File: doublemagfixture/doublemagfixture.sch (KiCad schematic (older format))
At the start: 36 parts, among them J1 Barrel_Jack_MountingPin, J2 Screw_Terminal_01x04, J3 Screw_Terminal_01x04, J4 Screw_Terminal_01x04, J5 Screw_Terminal_01x04, J6 Screw_Terminal_01x08, J7 Screw_Terminal_01x08, M1 12V_350mA_Stepper_Motor, M2 12V_350mA_Stepper_Motor, M3 12V_350mA_Stepper_Motor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

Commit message: almost done pcb
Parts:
- added H1, H2, H3: MountingHole, MountingHole:MountingHole_3.2mm_M3_Pad, symbol Mechanical:MountingHole
- D1: value DIR_IND -> DIR0
- D2: value DIR_IND -> DIR1
- D3: value STEP_IND -> STEP0
- D4: value STEP_IND -> STEP1
- D5: value DIR_IND -> DIR2
- D6: value DIR_IND -> DIR3
- D7: value STEP_IND -> STEP2
- D8: value STEP_IND -> STEP3
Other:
- note added: "to fixture"
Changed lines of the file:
@@
 EESchema Schematic File Version 4
-LIBS:doublemagfixture-cache
 EELAYER 30 0
 EELAYER END
@@
 P 7450 1100
 F 0 "D1" H 7450 893 50  0000 C CNN
-F 1 "DIR_IND" H 7450 984 50  0000 C CNN
+F 1 "DIR0" H 7450 984 50  0000 C CNN
 F 2 "LED_THT:LED_D3.0mm" V 7450 1100 50  0001 C CNN
 F 3 "~" V 7450 1100 50  0001 C CNN
@@
 P 7450 1200
 F 0 "D3" H 7450 1400 50  0000 C CNN
-F 1 "STEP_IND" H 7450 1300 50  0000 C CNN
+F 1 "STEP0" H 7450 1300 50  0000 C CNN
 F 2 "LED_THT:LED_D3.0mm" V 7450 1200 50  0001 C CNN
 F 3 "~" V 7450 1200 50  0001 C CNN
@@
 P 10750 1100
 F 0 "D2" H 10750 893 50  0000 C CNN
-F 1 "DIR_IND" H 10750 984 50  0000 C CNN
+F 1 "DIR1" H 10750 984 50  0000 C CNN
 F 2 "LED_THT:LED_D3.0mm" V 10750 1100 50  0001 C CNN
 F 3 "~" V 10750 1100 50  0001 C CNN
@@
 P 10750 1200
 F 0 "D4" H 10750 1400 50  0000 C CNN
-F 1 "STEP_IND" H 10750 1300 50  0000 C CNN
+F 1 "STEP1" H 10750 1300 50  0000 C CNN
 F 2 "LED_THT:LED_D3.0mm" V 10750 1200 50  0001 C CNN
 F 3 "~" V 10750 1200 50  0001 C CNN
@@
 P 7500 3700
 F 0 "D5" H 7500 3493 50  0000 C CNN
-F 1 "DIR_IND" H 7500 3584 50  0000 C CNN
+F 1 "DIR2" H 7500 3584 50  0000 C CNN
 F 2 "LED_THT:LED_D3.0mm" V 7500 3700 50  0001 C CNN
 F 3 "~" V 7500 3700 50  0001 C CNN
@@
 P 7500 3800
 F 0 "D7" H 7500 4000 50  0000 C CNN
-F 1 "STEP_IND" H 7500 3900 50  0000 C CNN
+F 1 "STEP2" H 7500 3900 50  0000 C CNN
 F 2 "LED_THT:LED_D3.0mm" V 7500 3800 50  0001 C CNN
 F 3 "~" V 7500 3800 50  0001 C CNN
@@
 P 10800 3700
 F 0 "D6" H 10800 3493 50  0000 C CNN
-F 1 "DIR_IND" H 10800 3584 50  0000 C CNN
+F 1 "DIR3" H 10800 3584 50  0000 C CNN
 F 2 "LED_THT:LED_D3.0mm" V 10800 3700 50  0001 C CNN
 F 3 "~" V 10800 3700 50  0001 C CNN
@@
 P 10800 3800
 F 0 "D8" H 10800 4000 50  0000 C CNN
-F 1 "STEP_IND" H 10800 3900 50  0000 C CNN
+F 1 "STEP3" H 10800 3900 50  0000 C CNN
 F 2 "LED_THT:LED_D3.0mm" V 10800 3800 50  0001 C CNN
 F 3 "~" V 10800 3800 50  0001 C CNN
@@
 Text Notes 1650 3600 2    50   ~ 0
 to limit switch
+Text Notes 5350 3000 0    50   ~ 0
+to fixture
+Text Notes 5400 5600 0    50   ~ 0
+to fixture
+Text Notes 8700 5600 0    50   ~ 0
+to fixture
+Text Notes 8650 3000 0    50   ~ 0
+to fixture
+$Comp
+L Mechanical:MountingHole H1
+U 1 1 61660AAE
+P 700 700
+F 0 "H1" H 800 746 50  0000 L CNN
+F 1 "MountingHole" H 800 655 50  0000 L CNN
+F 2 "MountingHole:MountingHole_3.2mm_M3_Pad" H 700 700 50  0001 C CNN
+F 3 "~" H 700 700 50  0001 C CNN
+	1    700  700
+	1    0    0    -1
+$EndComp
+$Comp
+L Mechanical:MountingHole H2
+U 1 1 6166153D
+P 700 950
+F 0 "H2" H 800 996 50  0000 L CNN
+F 1 "MountingHole" H 800 905 50  0000 L CNN
+F 2 "MountingHole:MountingHole_3.2mm_M3_Pad" H 700 950 50  0001 C CNN
+F 3 "~" H 700 950 50  0001 C CNN
+	1    700  950
+	1    0    0    -1
+$EndComp
+$Comp
+L Mechanical:MountingHole H3
+U 1 1 616617E1
+P 700 1200
+F 0 "H3" H 800 1246 50  0000 L CNN
+F 1 "MountingHole" H 800 1155 50  0000 L CNN
+F 2 "MountingHole:MountingHole_3.2mm_M3_Pad" H 700 1200 50  0001 C CNN
+F 3 "~" H 700 1200 50  0001 C CNN
+	1    700  1200
+	1    0    0    -1
+$EndComp
 $EndSCHEMATC

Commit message: Final(?) pcb
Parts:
- renumbered M3 to M2, M2 to M3
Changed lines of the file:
@@
 	2550 6900 2650 6900
 Connection ~ 2650 6900
-Wire Wire Line
-	2650 6900 2750 6900
 $Comp
 L Motor:Stepper_Motor_bipolar M1
@@
 $EndComp
 Wire Wire Line
-	8850 1100 8450 1100
-Wire Wire Line
 	8450 1100 8450 1000
 $Comp
@@
 	4950 2300 4500 2300
 $Comp
-L Motor:Stepper_Motor_bipolar M2
+L Motor:Stepper_Motor_bipolar M3
 U 1 1 619BDAE8
 P 4450 5400
-F 0 "M2" V 4650 5450 50  0000 R CNN
+F 0 "M3" V 4650 5450 50  0000 R CNN
 F 1 "12V_350mA_Stepper_Motor" V 4750 5900 50  0000 R CNN
 F 2 "" H 4460 5390 50  0001 C CNN
@@
 	8300 4900 7850 4900
 $Comp
-L Motor:Stepper_Motor_bipolar M3
+L Motor:Stepper_Motor_bipolar M2
 U 1 1 619CD0F7
 P 7700 2800
-F 0 "M3" V 7900 2850 50  0000 R CNN
+F 0 "M2" V 7900 2850 50  0000 R CNN
 F 1 "12V_350mA_Stepper_Motor" V 8000 3300 50  0000 R CNN
 F 2 "" H 7710 2790 50  0001 C CNN
@@
 	1    0    0    -1
 $EndComp
+Wire Wire Line
+	8850 1100 8450 1100
+Wire Wire Line
+	2750 6900 2650 6900
 $EndSCHEMATC

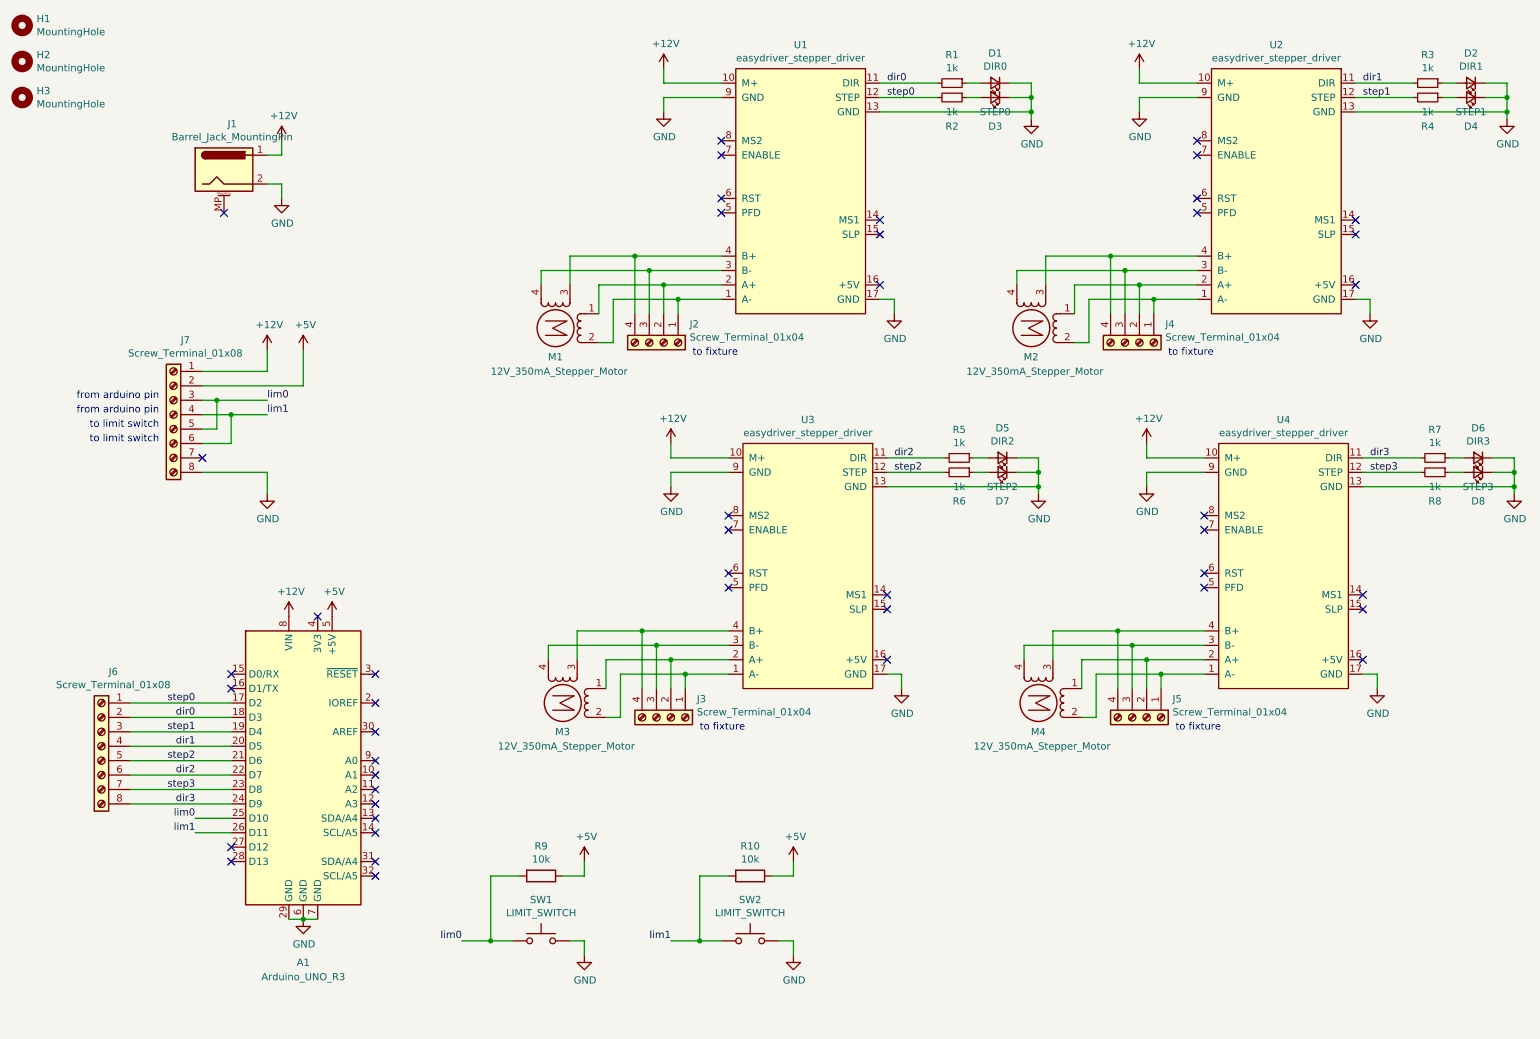
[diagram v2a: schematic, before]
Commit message: numbering fixes and wider traces on power line
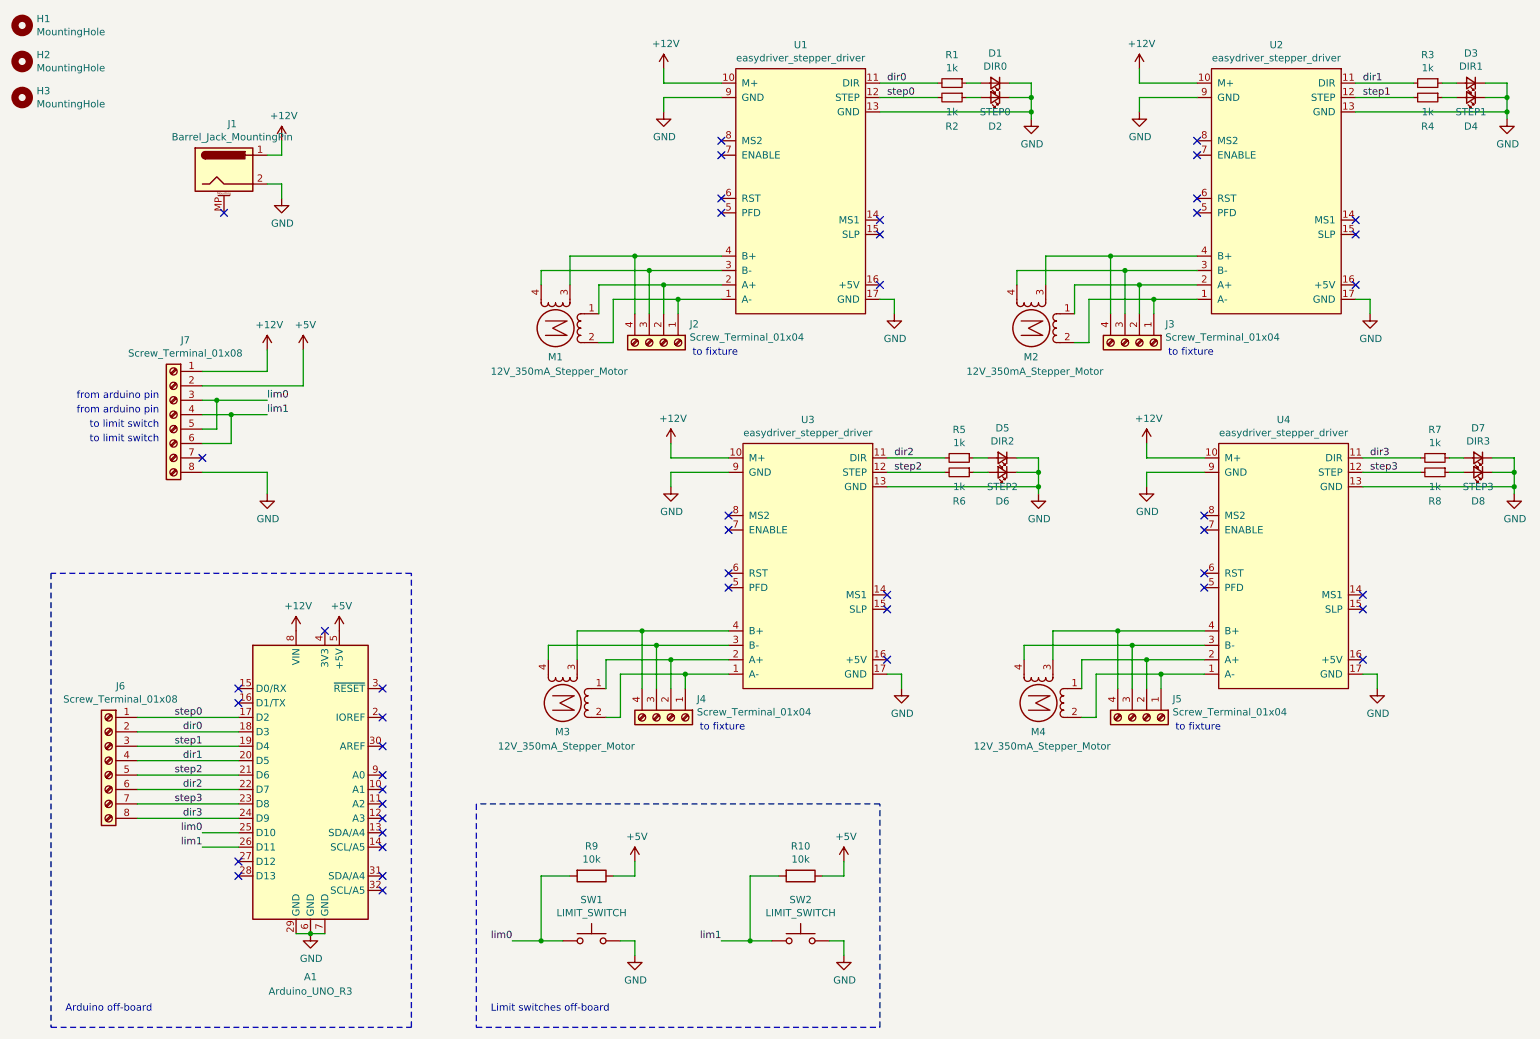
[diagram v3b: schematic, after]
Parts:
- renumbered D3 to D2, D2 to D3, D7 to D6, D6 to D7, J4 to J3, J3 to J4
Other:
- note added: "Arduino off-board"
- note added: "Limit switches off-board"
- moved on the sheet: A1, J6, R10, R9, SW1, SW2

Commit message: change LED to 5mm
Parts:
- D1, D2, D3, D4, D5, D6, D7, D8: footprint LED_THT:LED_D3.0mm -> LED_THT:LED_D5.0mm
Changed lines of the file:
@@
 F 0 "D1" H 7450 893 50  0000 C CNN
 F 1 "DIR0" H 7450 984 50  0000 C CNN
-F 2 "LED_THT:LED_D3.0mm" V 7450 1100 50  0001 C CNN
+F 2 "LED_THT:LED_D5.0mm" V 7450 1100 50  0001 C CNN
 F 3 "~" V 7450 1100 50  0001 C CNN
 	1    7450 1100
@@
 F 0 "D2" H 7450 1400 50  0000 C CNN
 F 1 "STEP0" H 7450 1300 50  0000 C CNN
-F 2 "LED_THT:LED_D3.0mm" V 7450 1200 50  0001 C CNN
+F 2 "LED_THT:LED_D5.0mm" V 7450 1200 50  0001 C CNN
 F 3 "~" V 7450 1200 50  0001 C CNN
 	1    7450 1200
@@
 F 0 "D3" H 10750 893 50  0000 C CNN
 F 1 "DIR1" H 10750 984 50  0000 C CNN
-F 2 "LED_THT:LED_D3.0mm" V 10750 1100 50  0001 C CNN
+F 2 "LED_THT:LED_D5.0mm" V 10750 1100 50  0001 C CNN
 F 3 "~" V 10750 1100 50  0001 C CNN
 	1    10750 1100
@@
 F 0 "D4" H 10750 1400 50  0000 C CNN
 F 1 "STEP1" H 10750 1300 50  0000 C CNN
-F 2 "LED_THT:LED_D3.0mm" V 10750 1200 50  0001 C CNN
+F 2 "LED_THT:LED_D5.0mm" V 10750 1200 50  0001 C CNN
 F 3 "~" V 10750 1200 50  0001 C CNN
 	1    10750 1200
@@
 F 0 "D5" H 7500 3493 50  0000 C CNN
 F 1 "DIR2" H 7500 3584 50  0000 C CNN
-F 2 "LED_THT:LED_D3.0mm" V 7500 3700 50  0001 C CNN
+F 2 "LED_THT:LED_D5.0mm" V 7500 3700 50  0001 C CNN
 F 3 "~" V 7500 3700 50  0001 C CNN
 	1    7500 3700
@@
 F 0 "D6" H 7500 4000 50  0000 C CNN
 F 1 "STEP2" H 7500 3900 50  0000 C CNN
-F 2 "LED_THT:LED_D3.0mm" V 7500 3800 50  0001 C CNN
+F 2 "LED_THT:LED_D5.0mm" V 7500 3800 50  0001 C CNN
 F 3 "~" V 7500 3800 50  0001 C CNN
 	1    7500 3800
@@
 F 0 "D7" H 10800 3493 50  0000 C CNN
 F 1 "DIR3" H 10800 3584 50  0000 C CNN
-F 2 "LED_THT:LED_D3.0mm" V 10800 3700 50  0001 C CNN
+F 2 "LED_THT:LED_D5.0mm" V 10800 3700 50  0001 C CNN
 F 3 "~" V 10800 3700 50  0001 C CNN
 	1    10800 3700
@@
 F 0 "D8" H 10800 4000 50  0000 C CNN
 F 1 "STEP3" H 10800 3900 50  0000 C CNN
-F 2 "LED_THT:LED_D3.0mm" V 10800 3800 50  0001 C CNN
+F 2 "LED_THT:LED_D5.0mm" V 10800 3800 50  0001 C CNN
 F 3 "~" V 10800 3800 50  0001 C CNN
 	1    10800 3800

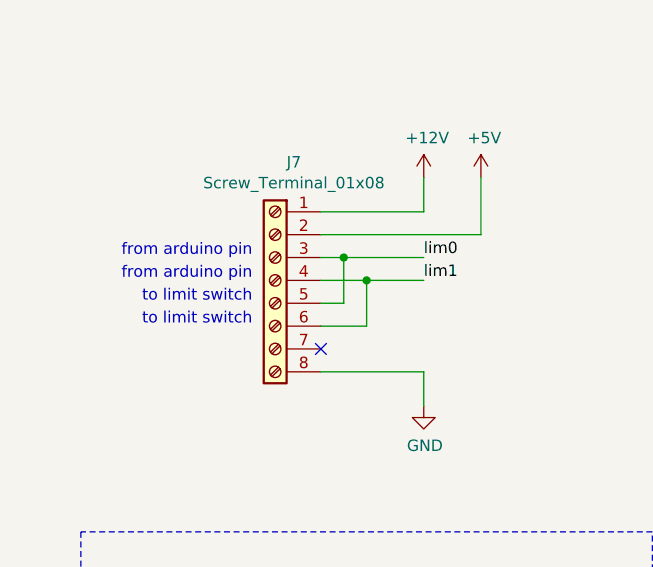
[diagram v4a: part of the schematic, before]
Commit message: add breakout board and reconfigure main board
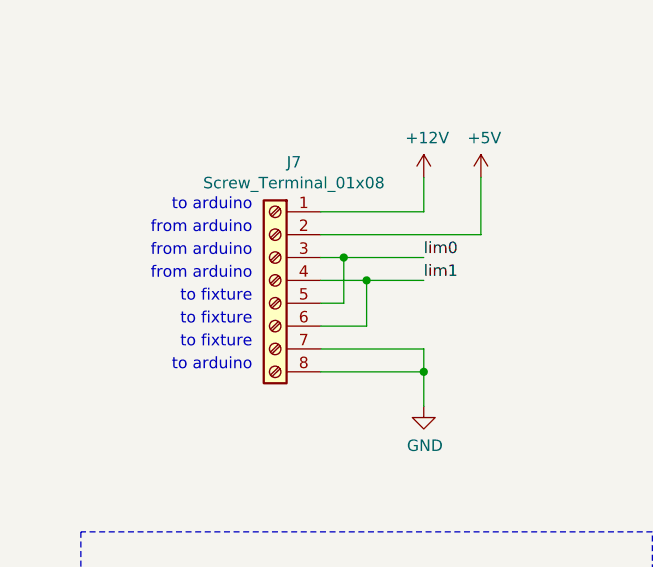
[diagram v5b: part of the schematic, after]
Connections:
- net GND: now also J7.7 (Pin_7)
- no-connect marks 46 -> 45
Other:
- note added: "from arduino"
- note added: "to arduino"
- note removed: "from arduino pin"
- note removed: "to limit switch"
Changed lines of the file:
@@
 Wire Wire Line
 	2150 3400 1950 3400
-NoConn ~ 1950 3700
 Text Notes 1650 3300 2    50   ~ 0
-from arduino pin
+from arduino
 Text Notes 1650 3400 2    50   ~ 0
-from arduino pin
+from arduino
 Text Notes 1650 3500 2    50   ~ 0
-to limit switch
+to fixture
 Text Notes 1650 3600 2    50   ~ 0
-to limit switch
+to fixture
 Text Notes 5350 3000 0    50   ~ 0
 to fixture
@@
 Wire Notes Line
 	900  7650 3400 7650
+Wire Wire Line
+	1950 3700 2400 3700
+Wire Wire Line
+	2400 3700 2400 3800
+Connection ~ 2400 3800
+Text Notes 1650 3700 2    50   ~ 0
+to fixture
+Text Notes 1650 3100 2    50   ~ 0
+to arduino
+Text Notes 1650 3200 2    50   ~ 0
+from arduino
+Text Notes 1650 3800 2    50   ~ 0
+to arduino
 $EndSCHEMATC

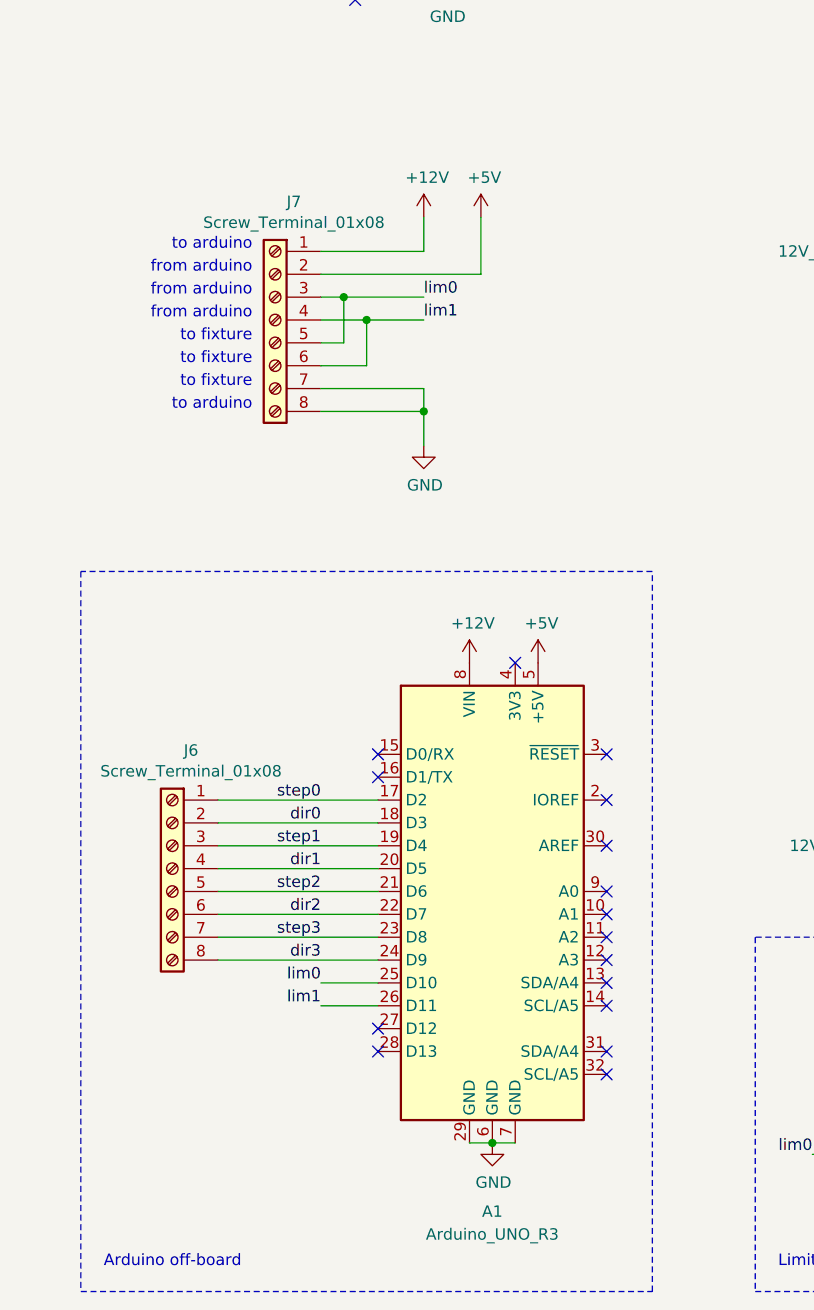
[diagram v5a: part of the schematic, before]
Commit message: add 3D mag work
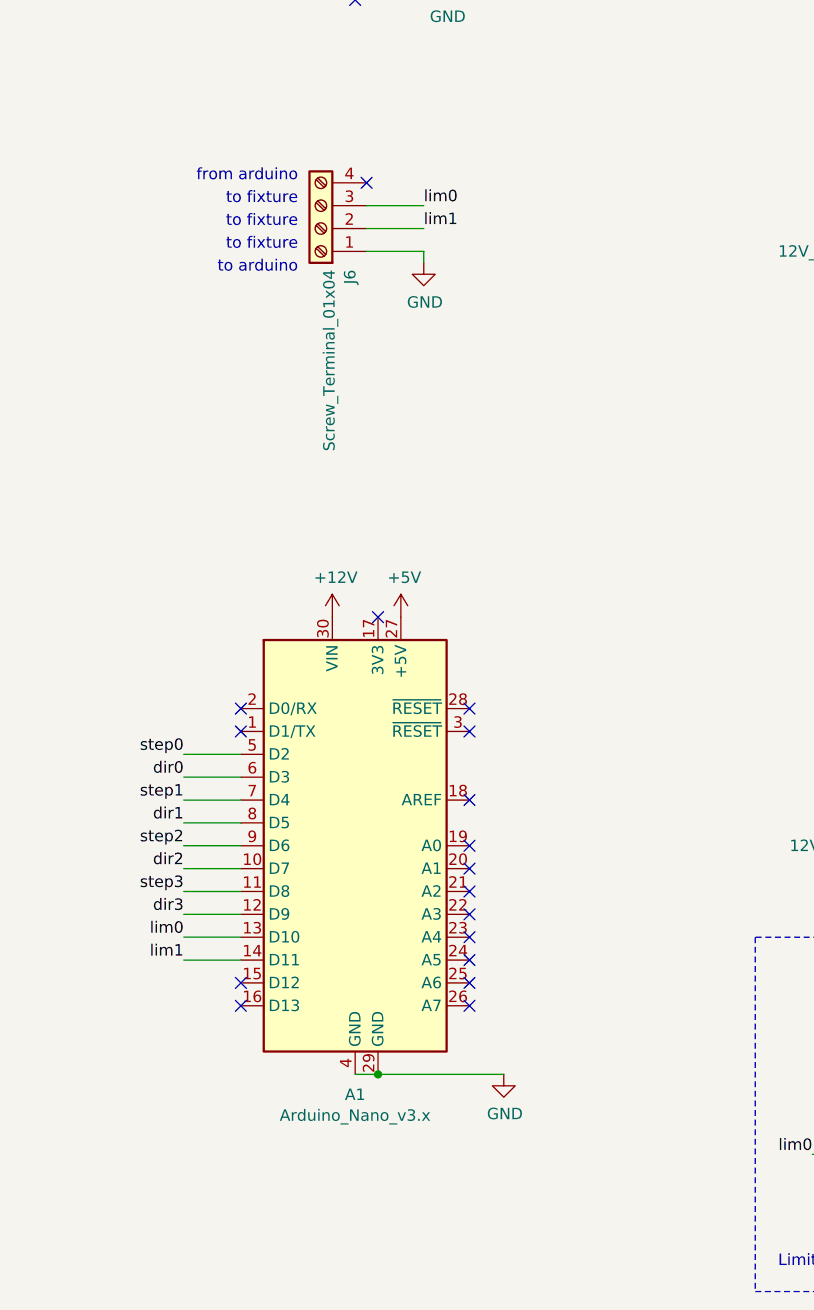
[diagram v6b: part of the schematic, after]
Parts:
- removed A1: Arduino_UNO_R3, symbol MCU_Module:Arduino_UNO_R3
- removed J6, J7: Screw_Terminal_01x08, doublemag:CONN_1x8_3.81mm, symbol Connector:Screw_Terminal_01x08
- added A1: Arduino_Nano_v3.x, Module:Arduino_Nano, symbol MCU_Module:Arduino_Nano_v3.x
- added J6: Screw_Terminal_01x04, doublemag:CONN_1x4_3.81mm, symbol Connector:Screw_Terminal_01x04
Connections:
- net +12V: now also A1.30 (VIN)
- net +5V: now also A1.27 (+5V)
- net GND: now also A1.29 (GND), A1.4 (GND), J6.1 (Pin_1)
- net dir0: now also A1.6 (D3)
- net dir1: now also A1.8 (D5)
- net dir2: now also A1.10 (D7)
- net dir3: now also A1.12 (D9)
- net lim0: now also A1.13 (D10), J6.3 (Pin_3)
- net lim1: now also A1.14 (D11), J6.2 (Pin_2)
- net step0: now also A1.5 (D2)
- net step1: now also A1.7 (D4)
- net step2: now also A1.9 (D6)
- net step3: now also A1.11 (D8)
- no-connect marks 45 -> 46
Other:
- note removed: "Arduino off-board"
